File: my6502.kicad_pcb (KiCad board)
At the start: 2 copper layers, 170 x 120 mm, 67 parts, among them J1 Conn_01x08, J2 Conn_01x08, J3 Conn_01x08, J4 USB_B_Micro, SW1 Switch, SW2 SW_MEC_5G, SW4 SW_Push, SW5 SW_Push, SW6 SW_Push, SW7 SW_Push, SW8 SW_Push, SW9 SW_Push, U1 74HC00, U12 74HC00, U17 74HC00, U18 LM555xN, U2 LM555xN, U3 W65C02S, U4 LM555xN, U5 28C256, U6 65C22, U7 CY62256-70PC, U8 HD44780, U9 74HC00, X1 CXO_DIP14

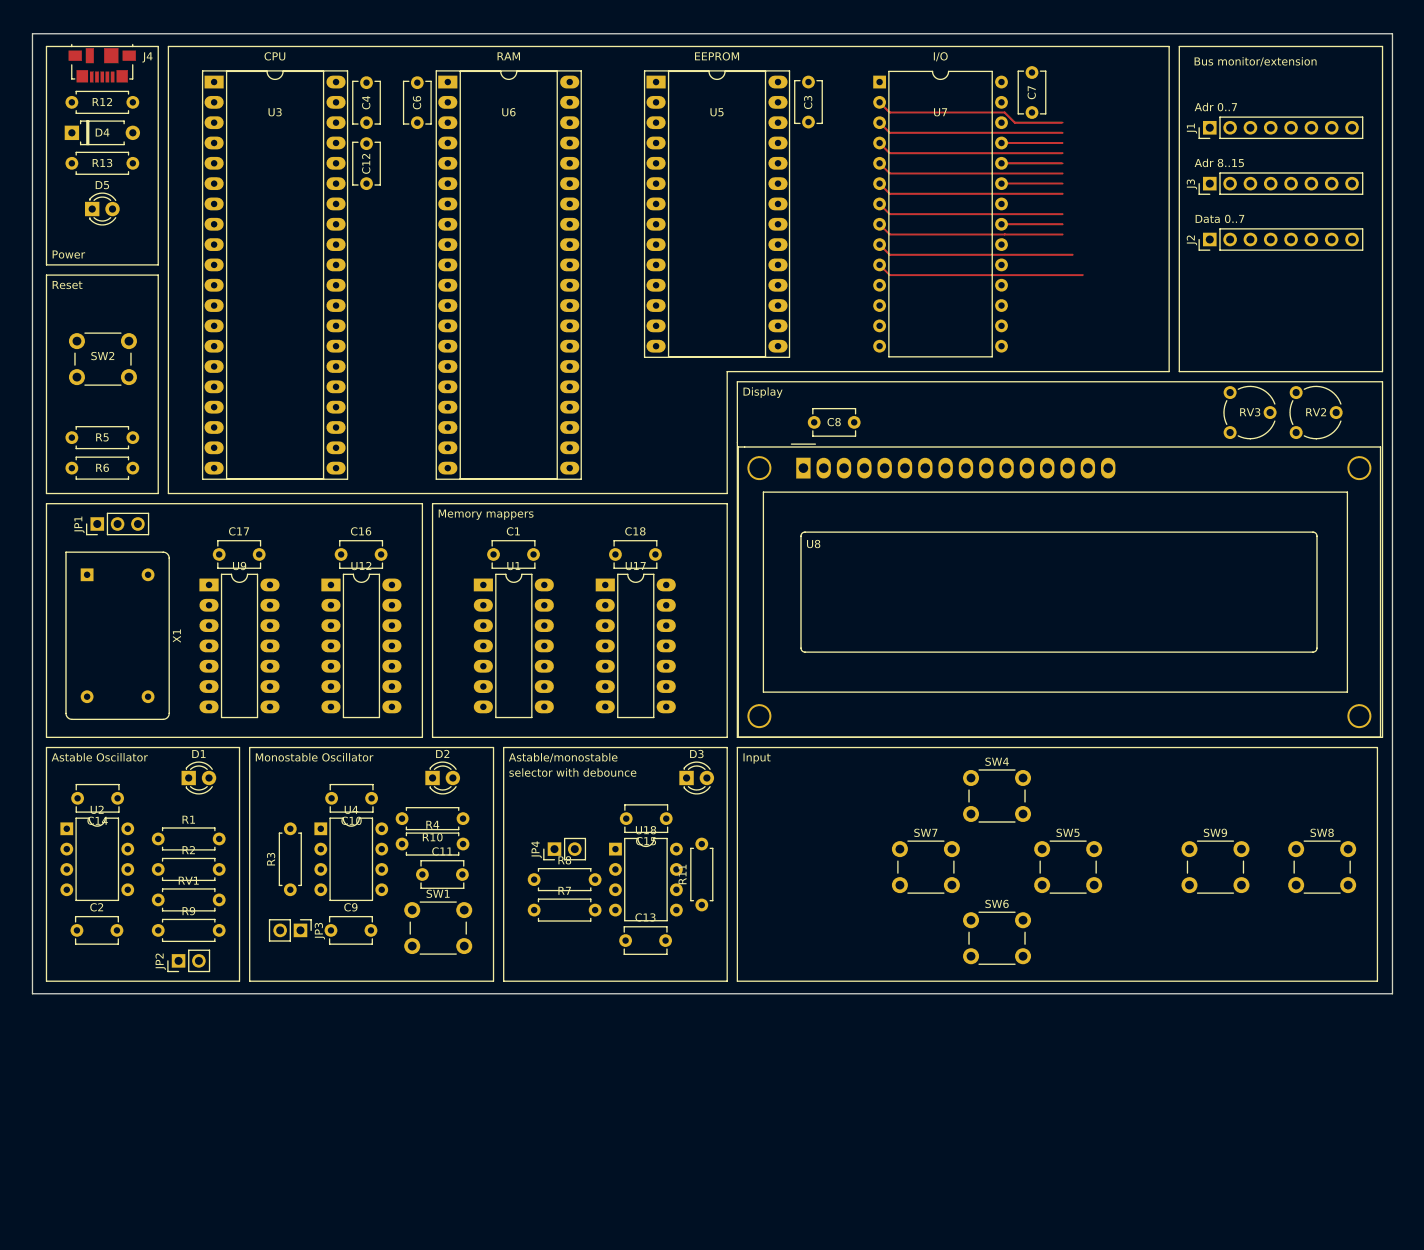
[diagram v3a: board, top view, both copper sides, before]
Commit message: Some components decided on and initial routing
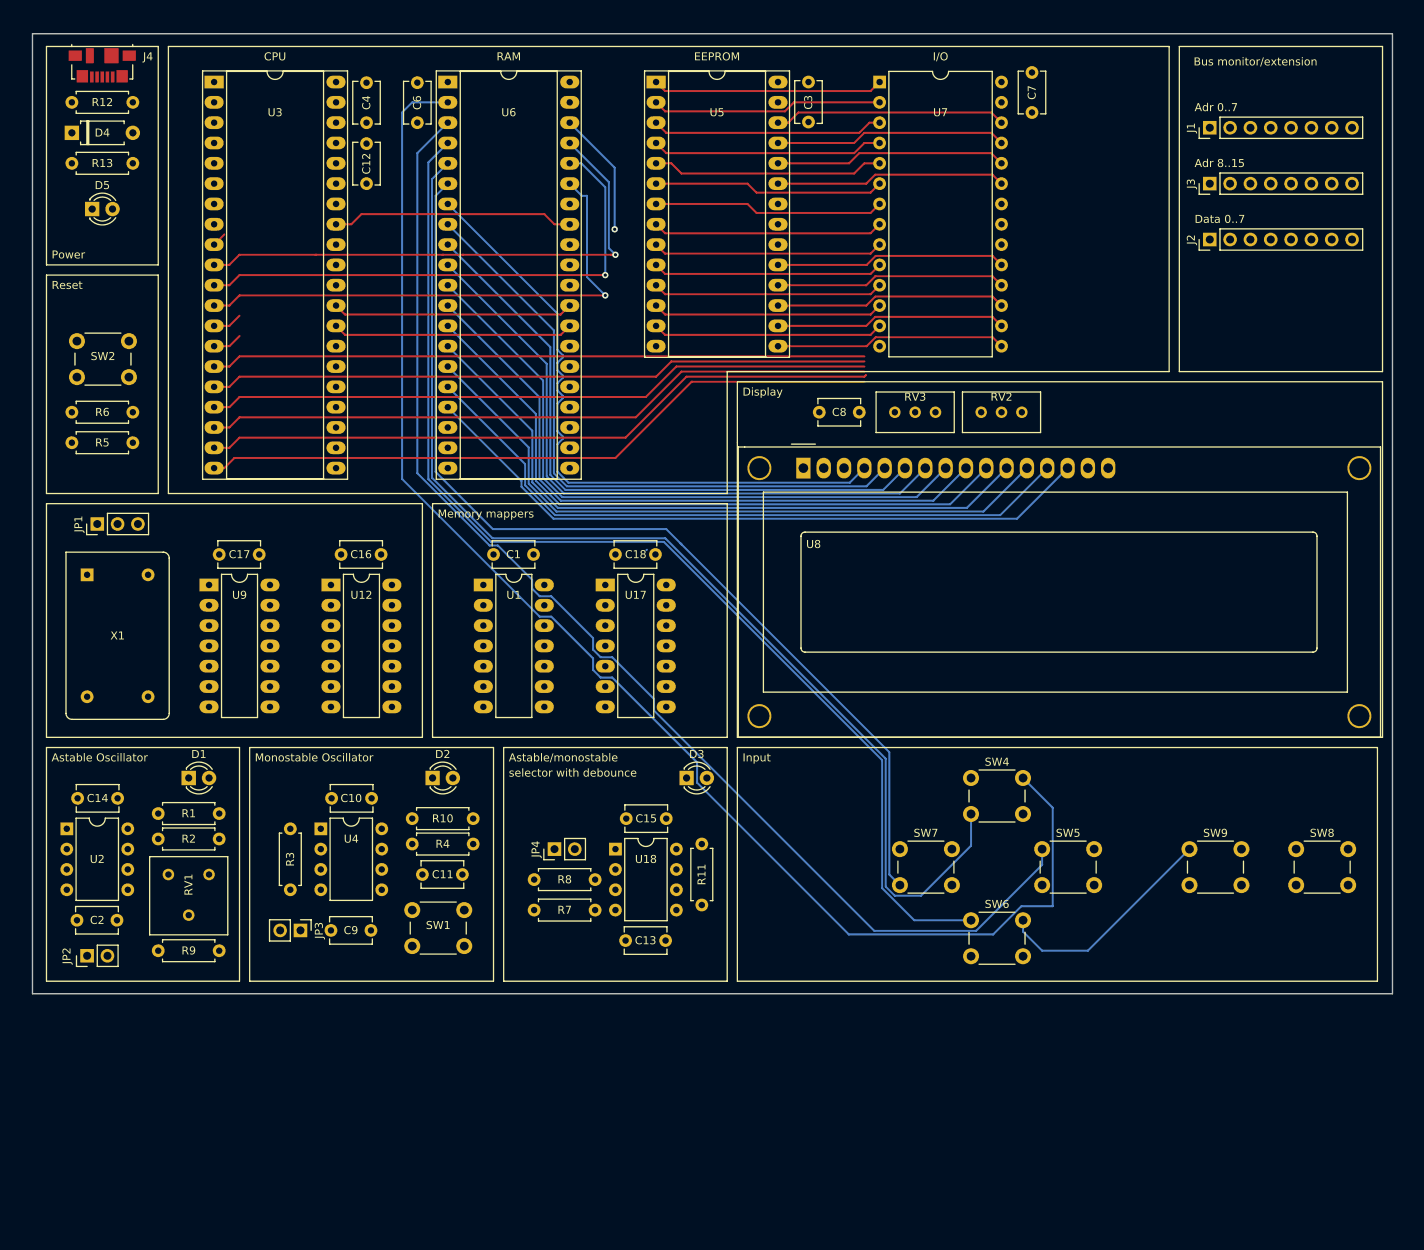
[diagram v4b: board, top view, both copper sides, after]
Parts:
- RV1: footprint Resistor_THT:R_Axial_DIN0207_L6.3mm_D2.5mm_P7.62mm_Horizontal -> Potentiometer_THT:Potentiometer_Bourns_3386F_Vertical
- RV2: footprint Potentiometer_THT:Potentiometer_Piher_PT-6-V_Vertical -> Potentiometer_THT:Potentiometer_Bourns_3296W_Vertical
- RV3: value 10k? -> 10k; footprint Potentiometer_THT:Potentiometer_Piher_PT-6-V_Vertical -> Potentiometer_THT:Potentiometer_Bourns_3296W_Vertical
- moved RV3 36.9 mm to (142.9, 67.3)
- moved RV2 34.4 mm to (153.7, 67.3)
- moved JP2 11.4 mm to (36.8, 135.3)
- moved R2 3.81 mm to (45.7, 120.7)
- moved RV1 3.42 mm to (47.0, 125.1), turned to 270 degrees
- moved R1 3.18 mm to (45.7, 117.5)
- moved R5 3.17 mm to (34.9, 71.1)
- moved R6 3.17 mm to (42.5, 67.3)
- moved R9 2.54 mm to (45.7, 134.6)
- moved C8 1.42 mm to (133.3, 67.3)
- moved C2 1.27 mm to (35.6, 130.8)
- moved R10 1.27 mm to (85.1, 118.1)
- moved R4 1.27 mm to (77.5, 121.3)
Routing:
- net /PA0: track 0.00 -> 178.3 mm
- net /PA2: track 0.00 -> 171.5 mm
- net /PA1: track 0.00 -> 154.9 mm
- net /PA3: track 0.00 -> 145.1 mm
- net /PA4: track 0.00 -> 125.4 mm
- net /A11: track 7.62 -> 114.6 mm
- net /A9: track 7.62 -> 113.2 mm
- net /A8: track 7.62 -> 112.4 mm
- net /A7: track 23.4 -> 111.6 mm
- net /A6: track 23.4 -> 110.8 mm
- net /PB7: track 0.00 -> 86.3 mm
- net /PB6: track 0.00 -> 85.6 mm
- net /PB5: track 0.00 -> 85.4 mm
- net /PB4: track 0.00 -> 84.1 mm
- net /PB3: track 0.00 -> 83.3 mm
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
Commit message: More routing
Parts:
- moved C12 29.2 mm to (101.0, 38.7)
- moved C4 29.2 mm to (101.0, 31.1)
- moved U3 29.2 mm to (81.9, 26.0)
- moved U6 26.7 mm to (55.2, 26.0)
- moved C6 26.7 mm to (51.4, 31.1)
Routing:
- net /PA0: track 178.3 -> 0.00 mm
- net /PA1: track 154.9 -> 0.00 mm
- net /PA3: track 145.1 -> 0.00 mm
- net /PA4: track 125.4 -> 0.08 mm
- net /PA2: track 171.5 -> 57.2 mm
- net /PA5: track 81.0 -> 2.58 mm
- net /D7: track 28.9 -> 107.0 mm, vias 0 -> 2
- net /PB7: track 86.3 -> 8.95 mm
- net /PB6: track 85.6 -> 8.31 mm
- net /PB5: track 85.4 -> 8.31 mm
- net /PB4: track 84.1 -> 7.04 mm
- net /PB3: track 83.3 -> 6.40 mm
- net /PB2: track 82.6 -> 5.76 mm
- net /PB1: track 81.8 -> 5.13 mm
- net /PB0: track 81.1 -> 4.49 mm
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
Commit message: many routes
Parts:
- moved C12 12.7 mm to (101.6, 26.0), turned to 270 degrees
- moved R10 7.62 mm to (77.5, 118.1), turned to 0 degrees
- moved R11 6.98 mm to (113.7, 121.9), turned to 270 degrees
- moved C1 5.08 mm to (92.7, 85.1), turned to 180 degrees
- moved C13 5.08 mm to (109.2, 133.3), turned to 180 degrees
- moved C16 5.08 mm to (73.7, 85.1), turned to 180 degrees
- moved C17 5.08 mm to (58.4, 85.1), turned to 180 degrees
- moved C18 5.08 mm to (108.0, 85.1), turned to 180 degrees
- moved C2 5.08 mm to (40.6, 130.8), turned to 180 degrees
- moved C9 5.08 mm to (72.4, 132.1), turned to 180 degrees
- moved C7 4.45 mm to (154.9, 25.4), turned to 270 degrees
- moved C4 2.62 mm to (101.6, 33.7), turned to 270 degrees
- moved C6 0.90 mm to (50.8, 30.5)
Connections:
- U17 pad 14: (no net) -> +5V
- U17 pad 7: (no net) -> GND
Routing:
- net +5V: track 0.00 -> 495.4 mm
- net /PA4: track 0.08 -> 257.6 mm
- net /PA3: track 0.00 -> 247.8 mm
- net /~A15: track 10.2 -> 252.6 mm, vias 0 -> 2
- net /PA1: track 0.00 -> 229.1 mm
- net /PA0: track 0.00 -> 211.1 mm
- net Net-(U17-Pad3): track 8.89 -> 189.3 mm, vias 0 -> 2
- net /PA2: track 57.2 -> 230.4 mm
- net CLK: track 0.00 -> 168.9 mm, vias 0 -> 2
- net /RWB: track 0.00 -> 135.3 mm, vias 0 -> 2
- net /RESET: track 0.00 -> 114.9 mm
- net /PA7: track 3.85 -> 117.1 mm
- net /PA6: track 3.22 -> 116.3 mm
- net /PA5: track 2.58 -> 115.4 mm
- net /PB7: track 8.95 -> 121.6 mm
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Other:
- copper layers 2 -> 4

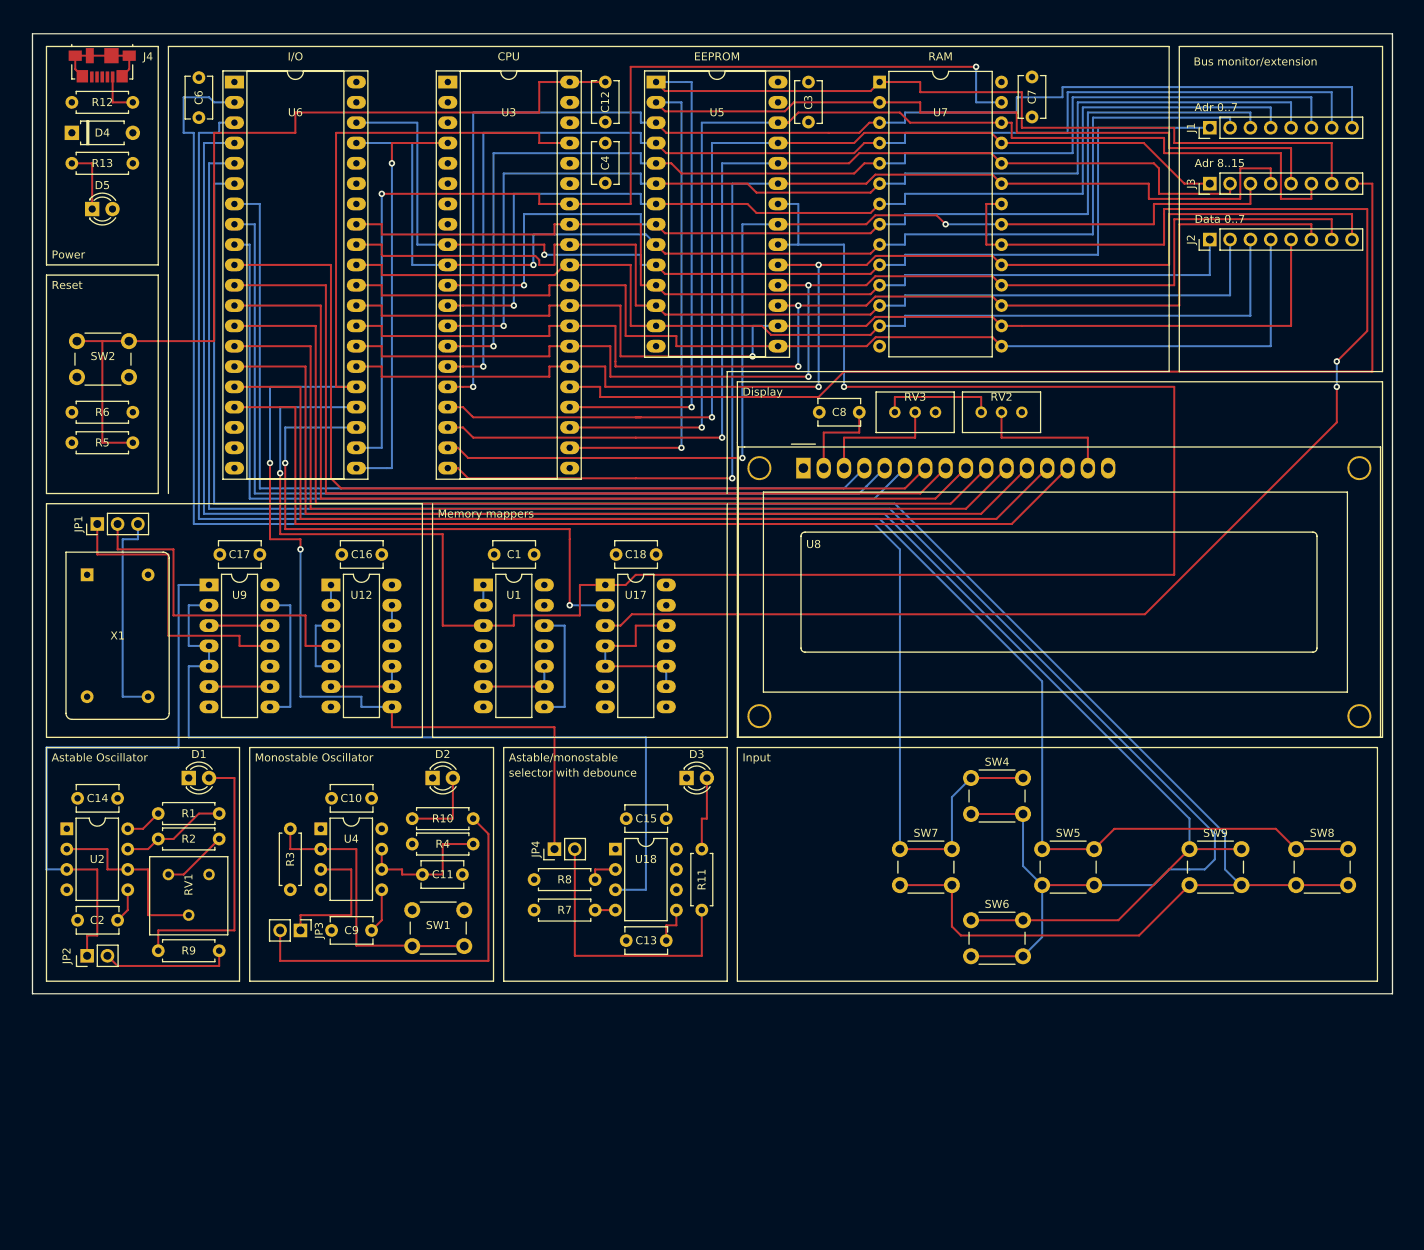
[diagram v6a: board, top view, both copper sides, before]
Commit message: only 3 routes remaining
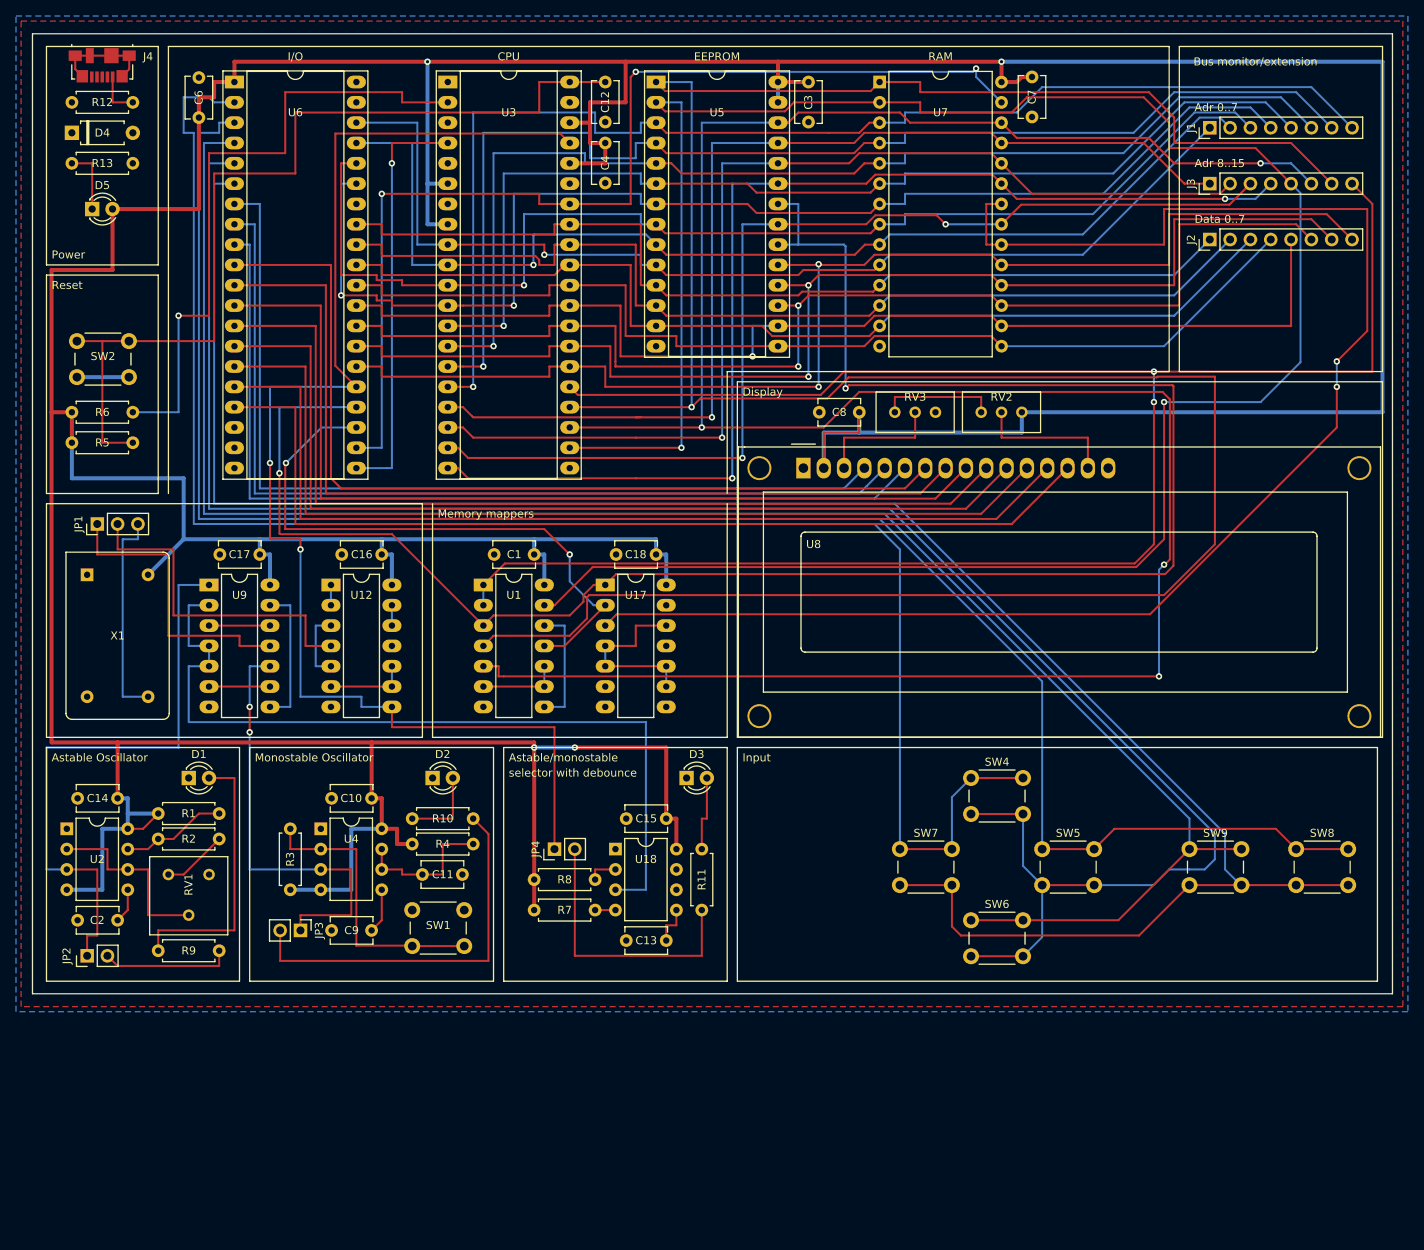
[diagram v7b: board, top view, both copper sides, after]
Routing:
- net +5V: track 495.4 -> 1041.1 mm, vias 0 -> 4
- net /A14: track 158.4 -> 339.8 mm
- net /A13: track 143.9 -> 317.4 mm, vias 1 -> 4
- net /A12: track 150.8 -> 289.0 mm, vias 1 -> 2
- net /A15: track 131.5 -> 237.5 mm, vias 0 -> 2
- net Net-(R6-Pad1): track 0.00 -> 80.6 mm, vias 0 -> 1
- net /MCLK: track 17.8 -> 54.6 mm, vias 0 -> 2
- net /A3: track 133.6 -> 156.3 mm, vias 1 -> 2
- net /A2: track 127.3 -> 149.2 mm
- net /A0: track 142.5 -> 132.6 mm
- net /A1: track 146.8 -> 136.9 mm
- net /~A15: track 252.6 -> 243.0 mm
- net /D3: track 138.7 -> 131.0 mm
- net /A4: track 140.0 -> 132.9 mm
- net GND: track 25.4 -> 31.9 mm
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- added copper zone on B.Cu, net GND
- added copper zone on F.Cu, net GND
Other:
- net class Power added: clearance 0.2, trace_width 0.5, via_dia 0.8, via_drill 0.4
